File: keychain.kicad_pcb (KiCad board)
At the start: 2 copper layers, 41 x 39 mm, 48 parts, among them P1 CAP_SLIDER, P2 VBAT, P3 CONN_01X04, P4 CONN_01X05, SW1 ~RESET~, SW2 BOOT, SW3 USR1, SW4 USR2, U1 EFM32TG110

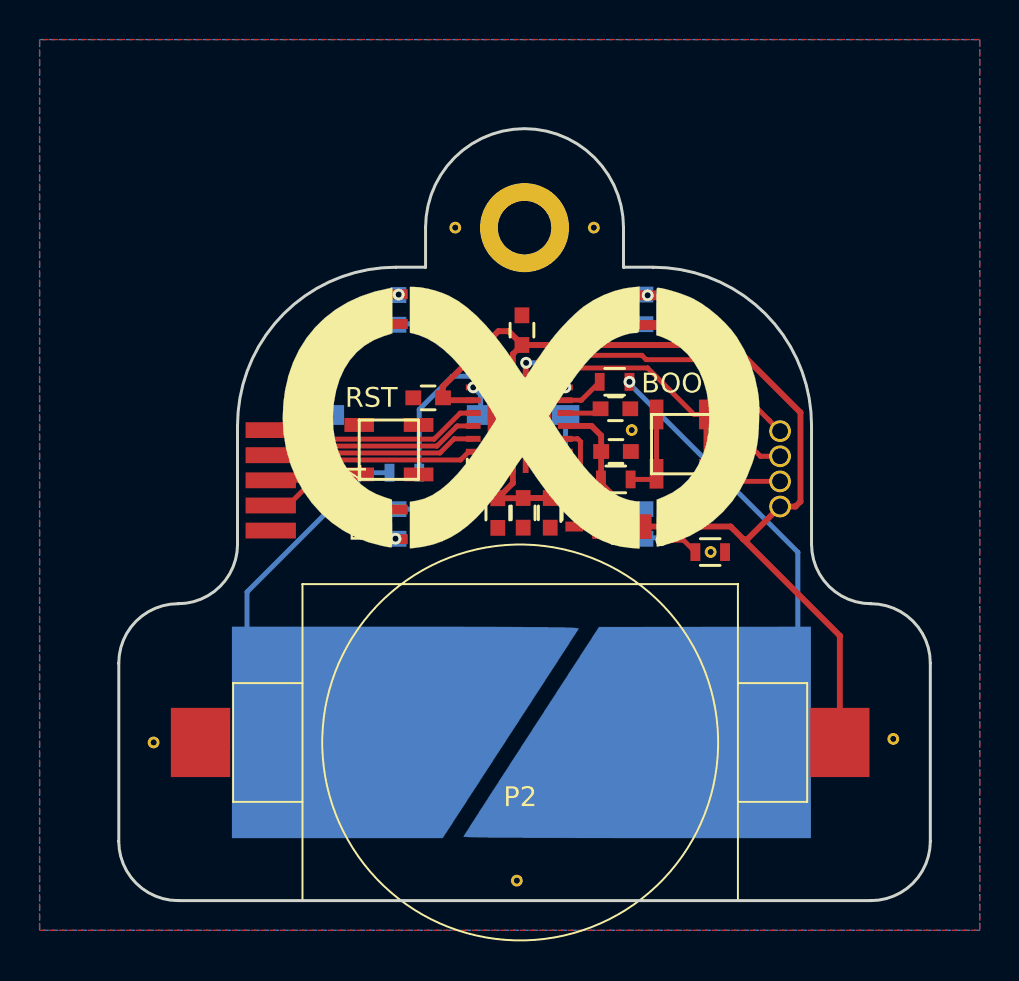
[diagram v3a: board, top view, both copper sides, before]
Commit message: Add 0R resistor for measuring current
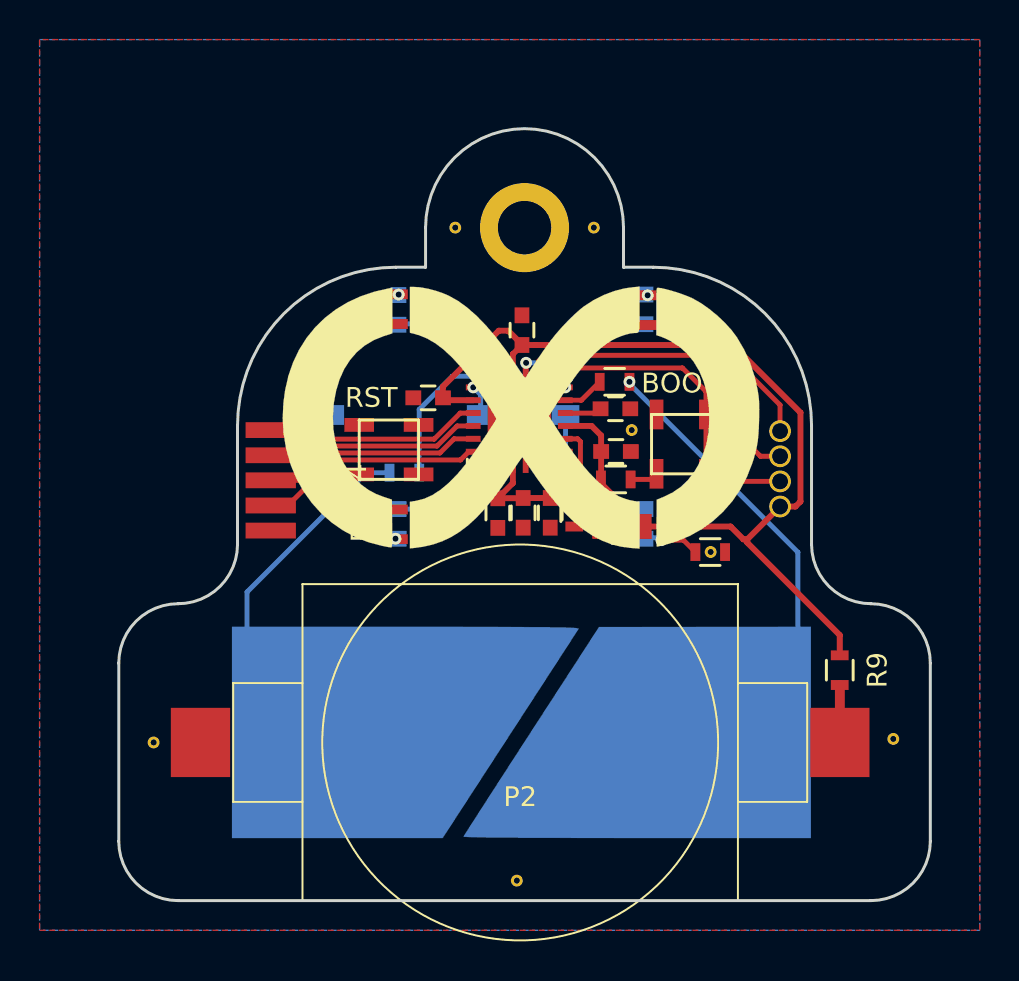
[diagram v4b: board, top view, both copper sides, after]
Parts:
- added R9: 0R, Resistors_SMD:R_0603, F.Cu at (165.4, 104.4)
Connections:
- P2 pad 2: +3V3 -> /VBAT
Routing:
- net +3V3: track 58.2 -> 53.7 mm
- net Net-(R1-Pad2): track 4.42 -> 1.42 mm
- net /VBAT: track 0.00 -> 2.91 mm
- net SWDIO: track 14.5 -> 15.3 mm
- net SWCLK: track 15.8 -> 16.5 mm
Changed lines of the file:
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@@
 (kicad_pcb (version 20160815) (host pcbnew "(2016-11-09 revision 58af5bc)-makepkg")
   (general
-    (links 79)
-    (no_connects 2)
-    (area 125 72.5 172.500001 118.160001)
+    (links 80)
+    (no_connects 4)
+    (area 128.924999 76.924999 170.075001 116.075001)
     (thickness 1.6)
     (drawings 20)
     (tracks 154)
     (zones 0)
-    (modules 48)
-    (nets 28)
+    (modules 49)
+    (nets 29)
   )
   (page A4)
@@
   (net 26 "Net-(SW3-Pad2)")
   (net 27 "Net-(SW4-Pad1)")
+  (net 28 /VBAT)
   (net_class Default "This is the default net class."
     (clearance 0.1)
@@
     (diff_pair_gap 0.25)
     (diff_pair_width 0.2)
+    (add_net /VBAT)
     (add_net /~RST~)
     (add_net CAP_S_1)
@@
       (net 2 GND))
     (pad 2 smd rect (at 16.15 0) (size 3 3.5) (layers F.Cu F.Paste F.Mask)
-      (net 1 +3V3))
+      (net 28 /VBAT))
   )
   (module keychain:silk_loop (layer F.Cu)
@@
       (net 2 GND))
   )
+  (module Resistors_SMD:R_0603 (layer F.Cu)
+    (at 165.42512 104.3566 270)
+    (descr "Resistor SMD 0603, reflow soldering, Vishay (see dcrcw.pdf)")
+    (tags "resistor 0603")
+    (attr smd)
+    (fp_text reference R9 (at 0 -1.9 270) (layer F.SilkS)
+      (effects (font (size 1 1) (thickness 0.15)))
+    )
+    (fp_text value 0R (at 0 1.9 270) (layer F.Fab)
+      (effects (font (size 1 1) (thickness 0.15)))
+    )
+    (fp_line (start -0.5 -0.675) (end 0.5 -0.675) (layer F.SilkS) (width 0.15))
+    (fp_line (start 0.5 0.675) (end -0.5 0.675) (layer F.SilkS) (width 0.15))
+    (fp_line (start 1.3 -0.8) (end 1.3 0.8) (layer F.CrtYd) (width 0.05))
+    (fp_line (start -1.3 -0.8) (end -1.3 0.8) (layer F.CrtYd) (width 0.05))
+    (fp_line (start -1.3 0.8) (end 1.3 0.8) (layer F.CrtYd) (width 0.05))
+    (fp_line (start -1.3 -0.8) (end 1.3 -0.8) (layer F.CrtYd) (width 0.05))
+    (pad 2 smd rect (at 0.75 0 270) (size 0.5 0.9) (layers F.Cu F.Paste F.Mask)
+      (net 28 /VBAT))
+    (pad 1 smd rect (at -0.75 0 270) (size 0.5 0.9) (layers F.Cu F.Paste F.Mask)
+      (net 1 +3V3))
+    (model Resistors_SMD.3dshapes/R_0603.wrl
+      (at (xyz 0 0 0))
+      (scale (xyz 1 1 1))
+      (rotate (xyz 0 0 0))
+    )
+  )
   (gr_arc (start 167 113) (end 170 113) (angle 90) (layer Edge.Cuts) (width 0.15))
   (gr_text BOOT (at 157.3657 89.8652) (layer F.SilkS)
@@
   (gr_arc (start 143 92) (end 135 92) (angle 90) (layer Edge.Cuts) (width 0.15))
   (gr_arc (start 156 92) (end 156 84) (angle 90) (layer Edge.Cuts) (width 0.15))
+  (segment (start 149.37 87.93) (end 149.37 87.905) (width 0.3) (layer F.Cu) (net 1))
+  (segment (start 149.37 87.905) (end 148.67336 87.20836) (width 0.3) (layer F.Cu) (net 1))
+  (segment (start 148.67336 87.20836) (end 148.197636 87.20836) (width 0.3) (layer F.Cu) (net 1))
+  (segment (start 148.197636 87.20836) (end 145.37 90.035996) (width 0.3) (layer F.Cu) (net 1))
   (segment (start 145.37 90.035996) (end 145.37 90.75) (width 0.3) (layer F.Cu) (net 1))
-  (segment (start 148.175996 87.23) (end 145.37 90.035996) (width 0.3) (layer F.Cu) (net 1))
-  (segment (start 148.695 87.23) (end 148.175996 87.23) (width 0.3) (layer F.Cu) (net 1))
-  (segment (start 149.37 87.905) (end 148.695 87.23) (width 0.3) (layer F.Cu) (net 1))
-  (segment (start 149.37 87.93) (end 149.37 87.905) (width 0.3) (layer F.Cu) (net 1))
-  (segment (start 165.43 102.62) (end 160.56 97.75) (width 0.3) (layer F.Cu) (net 1))
-  (segment (start 160.56 97.75) (end 159.91 97.1) (width 0.3) (layer F.Cu) (net 1))
+  (segment (start 160.749999 97.75) (end 160.749999 97.910399) (width 0.3) (layer F.Cu) (net 1))
+  (segment (start 160.749999 97.910399) (end 165.42512 102.58552) (width 0.3) (layer F.Cu) (net 1))
+  (segment (start 165.42512 102.58552) (end 165.42512 103.6066) (width 0.3) (layer F.Cu) (net 1))
   (segment (start 162.41 96.089999) (end 160.749999 97.75) (width 0.3) (layer F.Cu) (net 1))
-  (segment (start 160.749999 97.75) (end 160.56 97.75) (width 0.3) (layer F.Cu) (net 1))
   (segment (start 159.91 97.1) (end 155.42 97.1) (width 0.3) (layer F.Cu) (net 1))
-  (segment (start 165.43 108.01) (end 165.43 102.62) (width 0.3) (layer F.Cu) (net 1))
   (segment (start 162.41 96.089999) (end 163.187817 96.089999) (width 0.3) (layer F.Cu) (net 1))
   (segment (start 163.187817 96.089999) (end 163.44 95.837816) (width 0.3) (layer F.Cu) (net 1))
@@
   (segment (start 148.91 88.39) (end 149.37 87.93) (width 0.3) (layer F.Cu) (net 1))
   (segment (start 153.37 92.5) (end 152.89 92.02) (width 0.3) (layer F.Cu) (net 1))
+  (segment (start 160.56 97.75) (end 159.91 97.1) (width 0.3) (layer F.Cu) (net 1))
+  (segment (start 160.749999 97.75) (end 160.56 97.75) (width 0.3) (layer F.Cu) (net 1))
   (segment (start 159.62 98.4) (end 159.63 98.39) (width 0.25) (layer F.Cu) (net 2))
   (segment (start 162.41 93.549999) (end 161.419999 93.549999) (width 0.25) (layer F.Cu) (net 2))
@@
   (segment (start 151.56 91.37) (end 153.12 91.37) (width 0.25) (layer F.Cu) (net 3))
   (segment (start 153.12 91.37) (end 153.34 91.15) (width 0.25) (layer F.Cu) (net 3))
-  (segment (start 161.860001 91.729999) (end 162.41 92.279998) (width 0.25) (layer F.Cu) (net 5))
-  (segment (start 158.800001 88.669999) (end 161.860001 91.729999) (width 0.25) (layer F.Cu) (net 5))
-  (segment (start 155.64641 88.669999) (end 158.800001 88.669999) (width 0.25) (layer F.Cu) (net 5))
-  (segment (start 155.4264 88.449989) (end 155.64641 88.669999) (width 0.25) (layer F.Cu) (net 5))
+  (segment (start 150.21 89.37) (end 150.21 88.745) (width 0.25) (layer F.Cu) (net 5))
   (segment (start 150.21 88.745) (end 150.505011 88.449989) (width 0.25) (layer F.Cu) (net 5))
-  (segment (start 150.505011 88.449989) (end 155.4264 88.449989) (width 0.25) (layer F.Cu) (net 5))
-  (segment (start 150.21 89.37) (end 150.21 88.745) (width 0.25) (layer F.Cu) (net 5))
-  (segment (start 155.7184 89.0905) (end 151.5395 89.0905) (width 0.25) (layer F.Cu) (net 6))
+  (segment (start 150.505011 88.449989) (end 159.900189 88.449989) (width 0.25) (layer F.Cu) (net 5))
+  (segment (start 159.900189 88.449989) (end 162.4076 90.9574) (width 0.25) (layer F.Cu) (net 5))
+  (segment (start 162.4076 90.9574) (end 162.4076 92.277598) (width 0.25) (layer F.Cu) (net 5))
+  (segment (start 162.4076 92.277598) (end 162.41 92.279998) (width 0.25) (layer F.Cu) (net 5))
+  (segment (start 158.6665 91.4386) (end 158.6665 90.27954) (width 0.25) (layer F.Cu) (net 6))
   (segment (start 151.5395 89.0905) (end 151.26 89.37) (width 0.25) (layer F.Cu) (net 6))
+  (segment (start 158.6665 90.27954) (end 157.47746 89.0905) (width 0.25) (layer F.Cu) (net 6))
+  (segment (start 157.47746 89.0905) (end 151.5395 89.0905) (width 0.25) (layer F.Cu) (net 6))
   (segment (start 151.26 89.37) (end 150.86 89.37) (width 0.25) (layer F.Cu) (net 6))
-  (segment (start 158.6665 91.4386) (end 158.0665 91.4386) (width 0.25) (layer F.Cu) (net 6))
-  (segment (start 158.0665 91.4386) (end 155.7184 89.0905) (width 0.25) (layer F.Cu) (net 6))
   (segment (start 158.6665 94.4386) (end 158.6665 91.4386) (width 0.25) (layer F.Cu) (net 6))
   (segment (start 162.41 94.82) (end 159.0479 94.82) (width 0.25) (layer F.Cu) (net 6))
   (segment (start 159.0479 94.82) (end 158.6665 94.4386) (width 0.25) (layer F.Cu) (net 6))
-  (segment (start 156.1665 91.4386) (end 156.1665 92.4386) (width 0.25) (layer F.Cu) (net 7))
-  (segment (start 156.1665 92.4386) (end 156.1665 94.4386) (width 0.25) (layer F.Cu) (net 7))
   (segment (start 154.86 94.72) (end 155.8851 94.72) (width 0.25) (layer F.Cu) (net 7))
   (segment (start 155.8851 94.72) (end 156.1665 94.4386) (width 0.25) (layer F.Cu) (net 7))
@@
   (segment (start 151.5718 91.4654) (end 151.5718 94.0154) (width 0.25) (layer B.Cu) (net 27))
   (segment (start 151.5872 93.3472) (end 151.56 93.32) (width 0.25) (layer F.Cu) (net 27))
+  (segment (start 165.43 108.01) (end 165.43 105.11148) (width 0.5) (layer F.Cu) (net 28))
+  (segment (start 165.43 105.11148) (end 165.42512 105.1066) (width 0.25) (layer F.Cu) (net 28))
   (zone (net 2) (net_name GND) (layer F.Cu) (hatch edge 0.508)
     (connect_pads (clearance 0.3))
